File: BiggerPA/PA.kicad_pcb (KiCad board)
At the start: 2 copper layers, 100 x 100 mm, 105 parts, among them J1 Conn_Coaxial, J10 Conn_01x01, J2 Conn_01x02, J27 Conn_01x01, J28 Conn_01x01, J3 Conn_Coaxial, J4 Conn_01x02, J5 Conn_01x02, J6 Conn_01x01, J7 Conn_01x01, J8 Conn_01x01, J9 Conn_01x01, Q1 2N3906, Q10 IRF510N, Q11 IRF510N, Q12 IRF510N, Q13 IRF510N, Q14 IRF510N, Q15 IRF510N, Q18 TIP42, Q19 TIP42, Q2 IRF510N, Q20 TIP42, Q3 IRF510N, Q4 2N3906, Q5 TIP42, Q6 IRF510N, Q7 IRF510N, Q8 IRF510N, Q9 IRF510N, T1 Transformer_1P1Sdotted, T2 Transformer_1P1Sdotted, T3 Transformer_1P1Sdotted

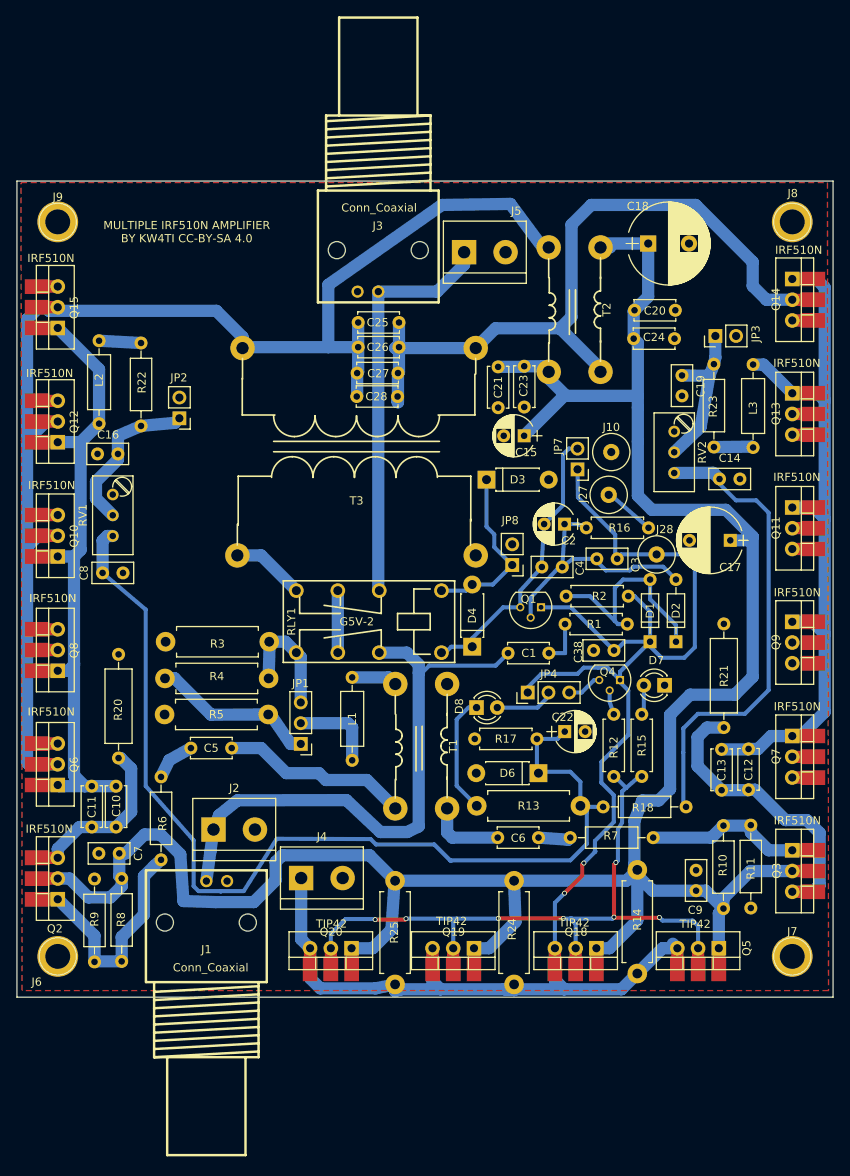
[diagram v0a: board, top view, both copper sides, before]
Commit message: Added series inductor to gates
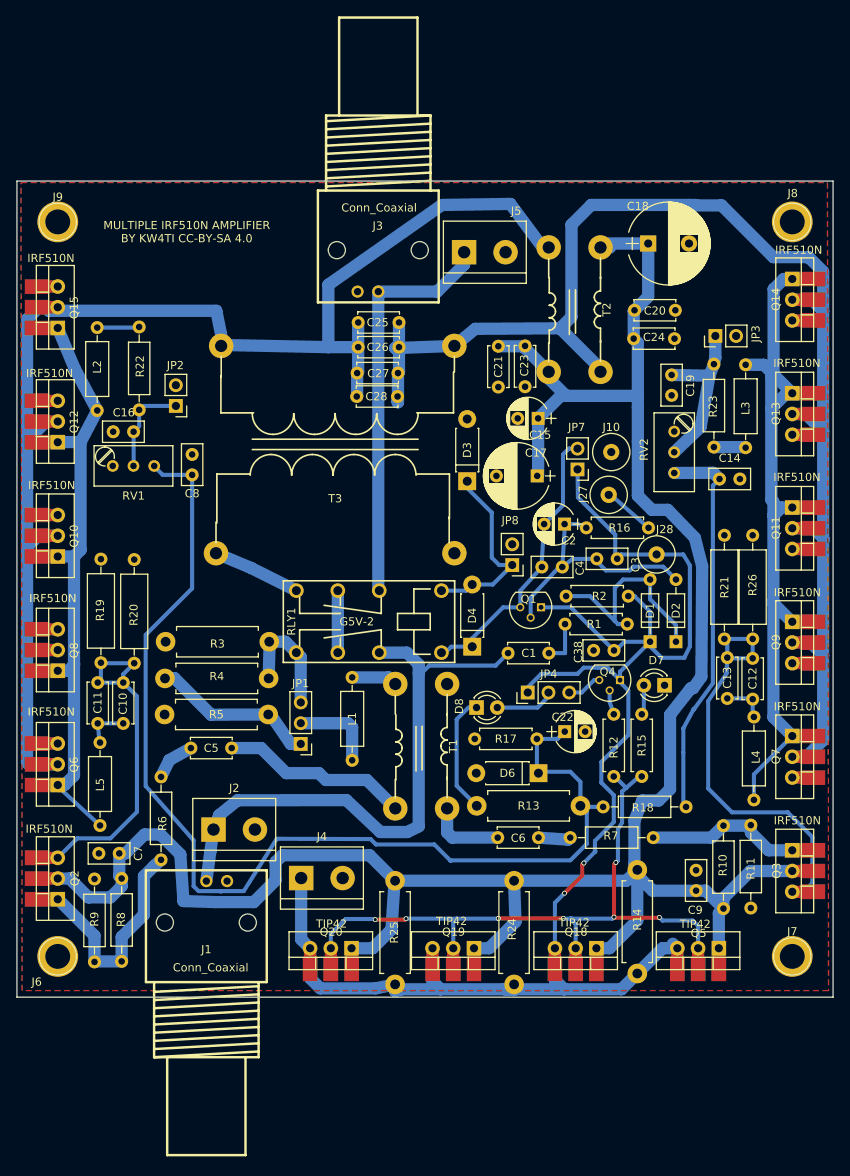
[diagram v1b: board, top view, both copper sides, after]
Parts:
- added L4: L, Inductors_THT:L_Axial_L6.6mm_D2.7mm_P10.16mm_Horizontal_Vishay_IM-2, F.Cu at (130.3, 105.7)
- added L5: L, Inductors_THT:L_Axial_L6.6mm_D2.7mm_P10.16mm_Horizontal_Vishay_IM-2, F.Cu at (50.2, 108.8)
- added R19: 51R, Resistors_THT:R_Axial_DIN0309_L9.0mm_D3.2mm_P12.70mm_Horizontal, F.Cu at (50.3, 99.0)
- added R26: 51R, Resistors_THT:R_Axial_DIN0309_L9.0mm_D3.2mm_P12.70mm_Horizontal, F.Cu at (130.1, 96.1)
- moved C17 24.9 mm to (103.7, 76.1)
- moved C8 16.3 mm to (61.5, 76.0), turned to 90 degrees
- moved R20 11.8 mm to (54.4, 99.1)
- moved R21 10.9 mm to (126.7, 96.1)
- moved C10 7.75 mm to (53.0, 106.5), turned to 90 degrees
- moved C11 7.73 mm to (49.9, 106.5), turned to 90 degrees
- moved C13 6.28 mm to (127.0, 103.4), turned to 90 degrees
- moved C12 6.12 mm to (130.1, 103.5), turned to 90 degrees
- moved RV1 3.51 mm to (51.7, 74.9), turned to 180 degrees
- moved C16 3.33 mm to (54.3, 70.7)
- moved C15 2.74 mm to (103.9, 69.1)
- moved T3 2.63 mm to (79.0, 72.9)
- moved C21 2.52 mm to (99.0, 60.2)
- moved C23 2.49 mm to (102.3, 60.2)
- moved D3 2.37 mm to (95.2, 76.8), turned to 90 degrees
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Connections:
- L2 pad 2: Net-(C10-Pad1) -> Net-(L2-Pad2)
- L3 pad 2: Net-(C12-Pad1) -> Net-(L3-Pad2)
- Q10 pad 1: Net-(C10-Pad1) -> Net-(L2-Pad2)
- Q11 pad 1: Net-(C12-Pad1) -> Net-(L3-Pad2)
- Q12 pad 1: Net-(C10-Pad1) -> Net-(L2-Pad2)
- Q13 pad 1: Net-(C12-Pad1) -> Net-(L3-Pad2)
- Q14 pad 1: Net-(C12-Pad1) -> Net-(L3-Pad2)
- Q15 pad 1: Net-(C10-Pad1) -> Net-(L2-Pad2)
- Q6 pad 1: Net-(C10-Pad1) -> Net-(L2-Pad2)
- Q7 pad 1: Net-(C12-Pad1) -> Net-(L3-Pad2)
- Q8 pad 1: Net-(C10-Pad1) -> Net-(L2-Pad2)
- Q9 pad 1: Net-(C12-Pad1) -> Net-(L3-Pad2)
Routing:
- net Net-(L3-Pad2): track 0.00 -> 97.9 mm
- net Net-(C12-Pad1): track 98.3 -> 5.40 mm
- net Net-(L2-Pad2): track 0.00 -> 86.7 mm
- net Net-(C25-Pad2): track 97.8 -> 182.1 mm
- net Net-(C10-Pad1): track 87.3 -> 5.51 mm
- net Net-(C10-Pad2): track 21.9 -> 43.9 mm
- net Net-(C12-Pad2): track 38.3 -> 54.5 mm
- net +5V: track 126.7 -> 138.3 mm
- net Net-(C14-Pad1): track 57.8 -> 48.4 mm
- net PASUPPLY: track 306.1 -> 296.8 mm
- net Net-(C16-Pad1): track 19.7 -> 11.9 mm
- net GND: track 22.9 -> 25.4 mm
- net AMPOUTPUT: track 9.02 -> 10.9 mm
- net Net-(D3-Pad1): track 21.7 -> 23.5 mm
- net Net-(C19-Pad1): track 19.2 -> 20.5 mm
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
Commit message: Added Filter
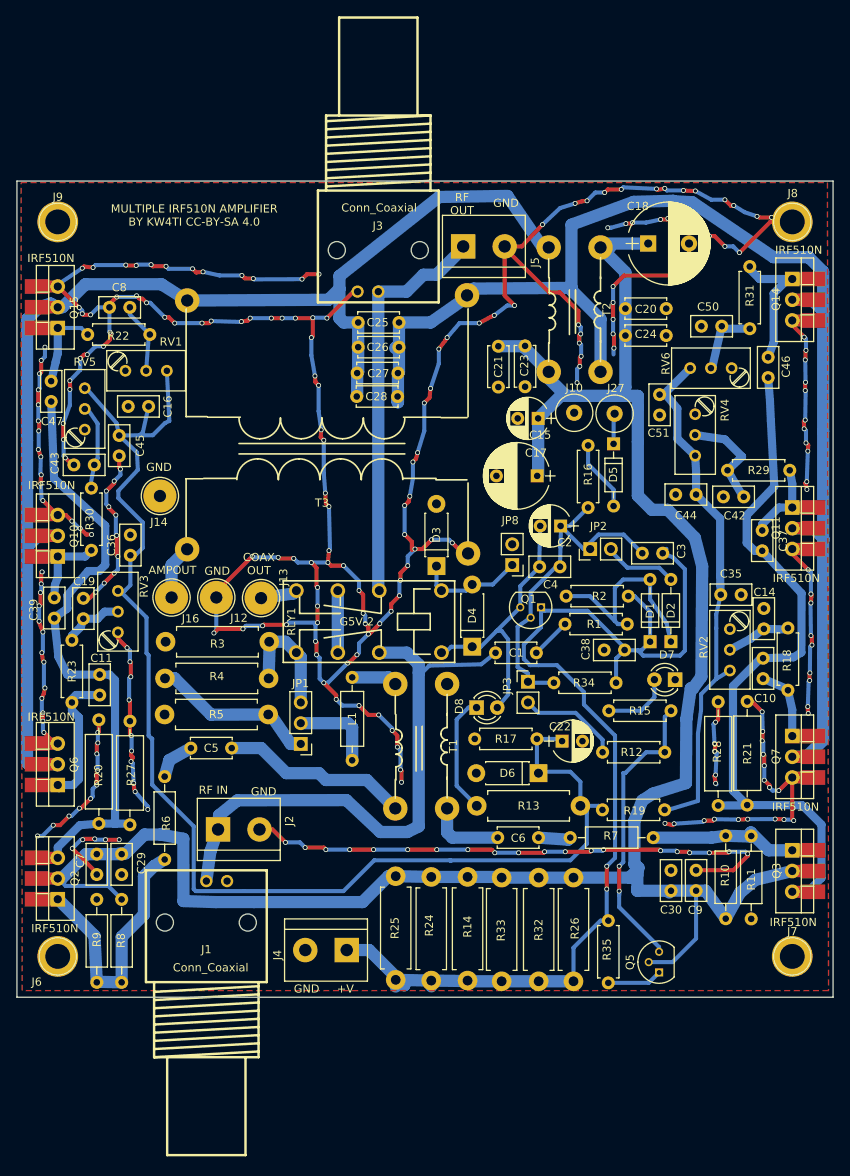
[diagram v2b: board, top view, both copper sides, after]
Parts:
- removed C12, C13: 100 nF, Capacitors_THT:C_Disc_D5.0mm_W2.5mm_P5.00mm
- removed J28: Conn_01x01, Connectors:1pin
- removed JP4: Jumper_NC_Dual, Pin_Headers:Pin_Header_Straight_1x03_Pitch2.54mm
- removed JP7: Jumper_NC_Small, Pin_Headers:Pin_Header_Straight_1x02_Pitch2.54mm
- removed L2, L3, L4, L5: L, Inductors_THT:L_Axial_L6.6mm_D2.7mm_P10.16mm_Horizontal_Vishay_IM-2
- removed Q12, Q13, Q8, Q9: IRF510N, PA:TO-220-3_Vertical_WithPads
- removed Q18, Q19, Q20: TIP42, PA:TO-220-3_Vertical_WithPads
- removed Q4: 2N3906, TO_SOT_Packages_THT:TO-92_Molded_Narrow
- added C29: 100 nF, Capacitors_THT:C_Disc_D5.0mm_W2.5mm_P2.50mm, F.Cu at (52.8, 125.0)
- added C30: 100 nF, Capacitors_THT:C_Disc_D5.0mm_W2.5mm_P2.50mm, F.Cu at (120.1, 124.5)
- added C35: 100 nF, Capacitors_THT:C_Disc_D5.0mm_W2.5mm_P2.50mm, F.Cu at (126.2, 90.7)
- added C36: 100 nF, Capacitors_THT:C_Disc_D5.0mm_W2.5mm_P2.50mm, F.Cu at (53.9, 85.9)
- added C37: 330 pF, Capacitors_THT:C_Disc_D5.0mm_W2.5mm_P2.50mm, F.Cu at (131.3, 82.8)
- added C39: 330 pF, Capacitors_THT:C_Disc_D5.0mm_W2.5mm_P2.50mm, F.Cu at (44.6, 91.1)
- added C42: 100 nF, Capacitors_THT:C_Disc_D5.0mm_W2.5mm_P2.50mm, F.Cu at (129.1, 78.7)
- added C43: 100 nF, Capacitors_THT:C_Disc_D5.0mm_W2.5mm_P2.50mm, F.Cu at (49.5, 74.8)
- added C44: 100 nF, Capacitors_THT:C_Disc_D5.0mm_W2.5mm_P2.50mm, F.Cu at (123.2, 78.4)
- added C45: 100 nF, Capacitors_THT:C_Disc_D5.0mm_W2.5mm_P2.50mm, F.Cu at (52.5, 71.2)
- added C46: 330 pF, Capacitors_THT:C_Disc_D5.0mm_W2.5mm_P2.50mm, F.Cu at (132.0, 61.6)
- added C47: 330 pF, Capacitors_THT:C_Disc_D5.0mm_W2.5mm_P2.50mm, F.Cu at (44.2, 64.5)
- added C50: 100 nF, Capacitors_THT:C_Disc_D5.0mm_W2.5mm_P2.50mm, F.Cu at (126.4, 57.8)
- added C51: 100 nF, Capacitors_THT:C_Disc_D5.0mm_W2.5mm_P2.50mm, F.Cu at (118.7, 66.2)
- added D5: 1N4148, Diodes_THT:D_DO-35_SOD27_P7.62mm_Horizontal, F.Cu at (113.1, 72.2)
- added J12: Conn_01x01, Connectors:1pin, F.Cu at (64.4, 91.0)
- added J13: Conn_01x01, Connectors:1pin, F.Cu at (69.9, 91.1)
- added J14: Conn_01x01, Connectors:1pin, F.Cu at (57.5, 78.6)
- added J16: Conn_01x01, Connectors:1pin, F.Cu at (58.9, 91.0)
- added R27: 51R, Resistors_THT:R_Axial_DIN0309_L9.0mm_D3.2mm_P12.70mm_Horizontal, F.Cu at (53.8, 118.9)
- added R28: 51R, Resistors_THT:R_Axial_DIN0309_L9.0mm_D3.2mm_P12.70mm_Horizontal, F.Cu at (125.9, 116.5)
- added R29: 10k, Resistors_THT:R_Axial_DIN0207_L6.3mm_D2.5mm_P7.62mm_Horizontal, F.Cu at (127.1, 75.4)
- added R30: 10k, Resistors_THT:R_Axial_DIN0207_L6.3mm_D2.5mm_P7.62mm_Horizontal, F.Cu at (49.1, 77.6)
- added R31: 10k, Resistors_THT:R_Axial_DIN0207_L6.3mm_D2.5mm_P7.62mm_Horizontal, F.Cu at (129.8, 58.1)
- added R32: 0R2, Resistors_THT:R_Axial_DIN0411_L9.9mm_D3.6mm_P12.70mm_Horizontal, F.Cu at (103.9, 125.3)
- added R33: 0R2, Resistors_THT:R_Axial_DIN0411_L9.9mm_D3.6mm_P12.70mm_Horizontal, F.Cu at (99.4, 125.3)
- added R34: 10k, Resistors_THT:R_Axial_DIN0207_L6.3mm_D2.5mm_P7.62mm_Horizontal, F.Cu at (113.4, 101.5)
- added R35: 470R, Resistors_THT:R_Axial_DIN0207_L6.3mm_D2.5mm_P7.62mm_Horizontal, F.Cu at (112.5, 130.6)
- added RV3: 10k, Potentiometers:Potentiometer_Trimmer_Bourns_3296W, F.Cu at (52.4, 95.3)
- added RV4: 10k, Potentiometers:Potentiometer_Trimmer_Bourns_3296W, F.Cu at (123.1, 68.6)
- added RV5: 10k, Potentiometers:Potentiometer_Trimmer_Bourns_3296W, F.Cu at (48.3, 70.5)
- added RV6: 10k, Potentiometers:Potentiometer_Trimmer_Bourns_3296W, F.Cu at (127.6, 62.9)
- C10, C11: value 100 nF -> 330 pF; footprint Capacitors_THT:C_Disc_D5.0mm_W2.5mm_P5.00mm -> Capacitors_THT:C_Disc_D5.0mm_W2.5mm_P2.50mm
- C15: value 1 uH -> 1 uF
- C17, C22: value 10 uH -> 10 uF
- C18: value 100 uH -> 100 uF
- C2: value 2.2 uH -> 2.2 uF
- Q5: value TIP42 -> 2N3906; footprint PA:TO-220-3_Vertical_WithPads -> TO_SOT_Packages_THT:TO-92_Molded_Narrow
- R12: value 10k -> 220R
- R13: value 2k4 -> 470R
- R18: value 0R -> 10k; footprint Resistors_THT:R_Axial_DIN0207_L6.3mm_D2.5mm_P10.16mm_Horizontal -> Resistors_THT:R_Axial_DIN0207_L6.3mm_D2.5mm_P7.62mm_Horizontal
- R19: value 51R -> 0R; footprint Resistors_THT:R_Axial_DIN0309_L9.0mm_D3.2mm_P12.70mm_Horizontal -> Resistors_THT:R_Axial_DIN0207_L6.3mm_D2.5mm_P7.62mm_Horizontal
- R22, R23: value 100R -> 10k; footprint Resistors_THT:R_Axial_DIN0207_L6.3mm_D2.5mm_P10.16mm_Horizontal -> Resistors_THT:R_Axial_DIN0207_L6.3mm_D2.5mm_P7.62mm_Horizontal
- R26: value 51R -> 0R2; footprint Resistors_THT:R_Axial_DIN0309_L9.0mm_D3.2mm_P12.70mm_Horizontal -> Resistors_THT:R_Axial_DIN0411_L9.9mm_D3.6mm_P12.70mm_Horizontal
- moved R23 82.1 mm to (46.7, 96.3), turned to 270 degrees
- moved C10 78.6 mm to (131.4, 101.0)
- moved C19 78.0 mm to (48.1, 93.6), turned to 90 degrees
- moved R19 71.4 mm to (119.4, 117.0), turned to 180 degrees
- moved JP2 53.7 mm to (110.2, 85.1), turned to 90 degrees
- moved JP3 48.2 mm to (102.6, 101.3), turned to 0 degrees
- moved R26 36.6 mm to (108.2, 125.3), turned to 270 degrees
- moved R18 25.2 mm to (134.5, 94.8), turned to 270 degrees
- moved RV2 25.1 mm to (127.4, 94.9)
- moved C8 21.9 mm to (53.8, 55.5), turned to 180 degrees
- moved R14 20.8 mm to (95.2, 125.3)
- moved R21 20.5 mm to (129.5, 116.5)
- moved R20 20.1 mm to (50.0, 118.7)
- moved C14 19.2 mm to (131.5, 94.9), turned to 90 degrees
- moved R16 12.5 mm to (110.0, 72.4), turned to 270 degrees
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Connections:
- C11 pad 1: Net-(C10-Pad1) -> Net-(C11-Pad1)
- C11 pad 2: Net-(C10-Pad2) -> Net-(C11-Pad2)
- C16 pad 1: Net-(C16-Pad1) -> +5V
- C3 pad 1: +28V -> +12V
- C38 pad 1: +28V -> +12V
- C8 pad 1: +5V -> Net-(C8-Pad1)
- D1 pad 1: +28V -> +12V
- D2 pad 2: Net-(C2-Pad1) -> Net-(D2-Pad2)
- D8 pad 2: Net-(D8-Pad2) -> Net-(C2-Pad2)
- J27 pad 1: Net-(J27-Pad1) -> Net-(D5-Pad1)
- J4 pad 1: +28V -> +12V
- JP2 pad 1: Net-(C16-Pad1) -> Net-(C2-Pad1)
- JP2 pad 2: GND -> Net-(D2-Pad2)
- JP3 pad 1: Net-(C19-Pad1) -> Net-(C2-Pad1)
- JP3 pad 2: GND -> Net-(JP3-Pad2)
- Q1 pad 1: +28V -> +12V
- Q10 pad 1: Net-(L2-Pad2) -> Net-(C39-Pad1)
- Q11 pad 1: Net-(L3-Pad2) -> Net-(C37-Pad1)
- Q14 pad 1: Net-(L3-Pad2) -> Net-(C46-Pad1)
- Q15 pad 1: Net-(L2-Pad2) -> Net-(C47-Pad1)
- Q2 pad 3: Net-(C10-Pad2) -> Net-(C11-Pad2)
- Q3 pad 3: Net-(C12-Pad2) -> Net-(C10-Pad2)
- Q5 pad 1: PASUPPLY -> Net-(Q5-Pad1)
- Q5 pad 2: Net-(Q18-Pad2) -> PASUPPLY
- Q5 pad 3: +28V -> Net-(Q5-Pad3)
- Q6 pad 1: Net-(L2-Pad2) -> Net-(C11-Pad1)
- Q7 pad 1: Net-(L3-Pad2) -> Net-(C10-Pad1)
- R12 pad 1: Net-(Q18-Pad2) -> Net-(JP3-Pad2)
- R12 pad 2: Net-(Q4-Pad2) -> Net-(Q5-Pad3)
- R14 pad 2: +28V -> +12V
- R15 pad 1: Net-(Q18-Pad2) -> Net-(Q5-Pad3)
- R16 pad 1: Net-(J27-Pad1) -> Net-(D5-Pad2)
- R18 pad 2: +5V -> Net-(C10-Pad1)
- R19 pad 1: Net-(C10-Pad2) -> Net-(C35-Pad1)
- R19 pad 2: GND -> +5V
- R2 pad 1: +28V -> +12V
- R20 pad 1: Net-(C10-Pad2) -> Net-(C11-Pad2)
- R21 pad 1: Net-(C12-Pad2) -> Net-(C10-Pad2)
- R22 pad 1: Net-(L2-Pad1) -> Net-(C8-Pad1)
- R22 pad 2: Net-(C16-Pad1) -> Net-(C47-Pad1)
- R23 pad 1: Net-(L3-Pad1) -> Net-(C19-Pad1)
- R23 pad 2: Net-(C19-Pad1) -> Net-(C11-Pad1)
- R24 pad 2: +28V -> +12V
- R25 pad 2: +28V -> +12V
- R26 pad 1: Net-(C12-Pad2) -> PASUPPLY
- R26 pad 2: GND -> +12V
- RLY1 pad 8: AMPOUTPUT -> COAXOUT
- RV1 pad 2: Net-(C16-Pad1) -> Net-(C8-Pad1)
- RV2 pad 2: Net-(C19-Pad1) -> Net-(C14-Pad1)
- RV2 pad 3: Net-(C14-Pad1) -> Net-(C35-Pad1)
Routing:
- net GND: track 25.4 -> 690.5 mm, vias 0 -> 255
- net +28V: track 206.0 -> 0.00 mm, vias 2 -> 0
- net +12V: track 0.00 -> 139.0 mm, vias 0 -> 2
- net Net-(L3-Pad2): track 97.9 -> 0.00 mm
- net Net-(Q18-Pad2): track 90.5 -> 0.00 mm, vias 7 -> 0
- net Net-(L2-Pad2): track 86.7 -> 0.00 mm
- net Net-(C11-Pad2): track 0.00 -> 77.6 mm
- net Net-(C35-Pad1): track 0.00 -> 65.4 mm
- net Net-(C12-Pad2): track 54.5 -> 0.00 mm
- net Net-(C10-Pad2): track 43.9 -> 90.7 mm
- net Net-(C14-Pad1): track 48.4 -> 7.90 mm
- net Net-(Q5-Pad3): track 0.00 -> 36.2 mm, vias 0 -> 2
- net PASUPPLY: track 296.8 -> 267.8 mm
- net +5V: track 138.3 -> 163.7 mm
- net Net-(C11-Pad1): track 0.00 -> 19.6 mm
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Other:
- board text added: "+V"
- board text added: "AMPOUT"
- board text added: "COAX OUT"
- board text added: "GND"
- board text added: "RF IN"
- board text added: "RF OUT"
- board text removed: "TIP42"

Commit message: Changed to 7805 regulator
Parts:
- removed D6: 1N4744A, Diodes_THT:D_DO-41_SOD81_P7.62mm_Horizontal
- removed R13: 470R, Resistors_THT:R_Axial_DIN0411_L9.9mm_D3.6mm_P12.70mm_Horizontal
- added U1: LM7805_TO220, TO_SOT_Packages_THT:TO-220-3_Vertical, F.Cu at (100.2, 116.9)
- moved R12 1.48 mm to (112.2, 108.6)
- moved C22 0.22 mm to (106.9, 108.5)
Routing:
- net +5V: track 163.7 -> 158.9 mm
- net Net-(D8-Pad1): track 14.7 -> 16.8 mm
- net +12V: track 139.0 -> 140.8 mm
- net Net-(JP3-Pad2): track 12.6 -> 11.5 mm
- net Net-(Q5-Pad3): track 36.2 -> 35.1 mm
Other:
- board text added: "LM7805"

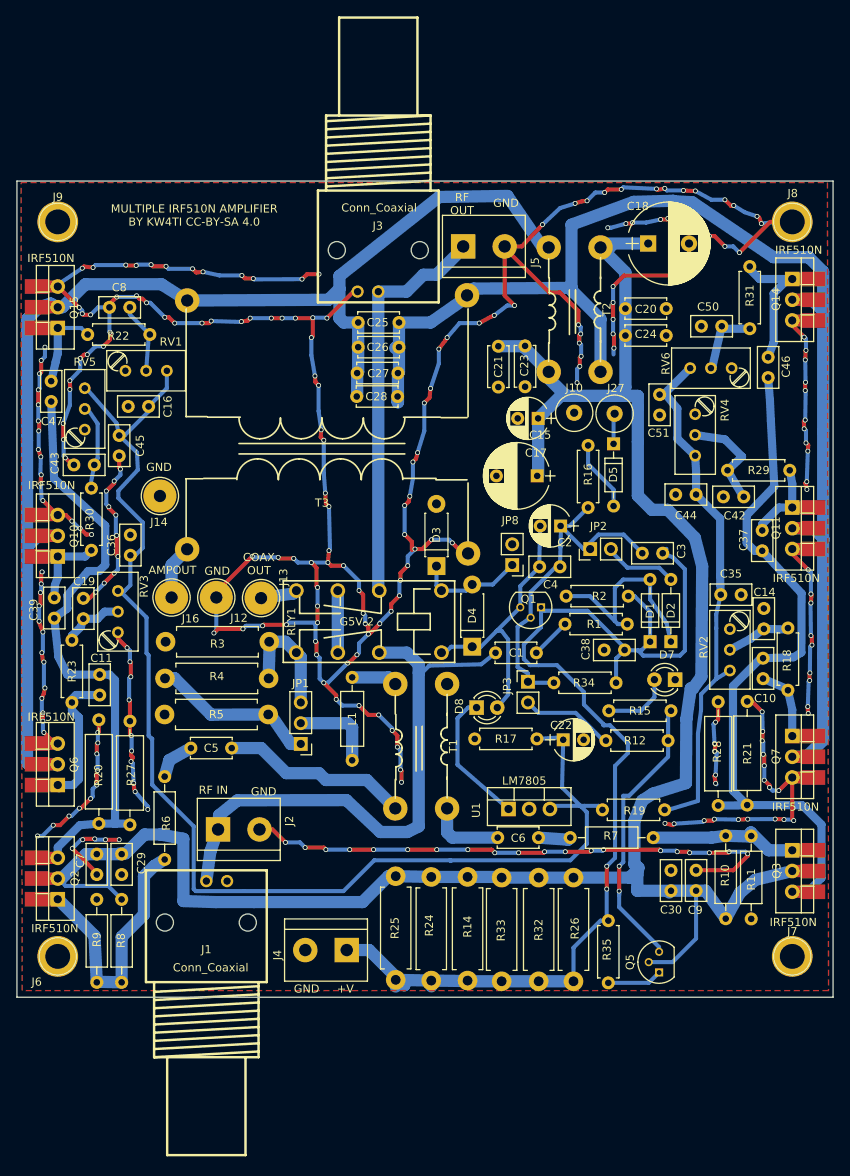
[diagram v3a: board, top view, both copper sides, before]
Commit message: Added gate resistors to BiggerPA
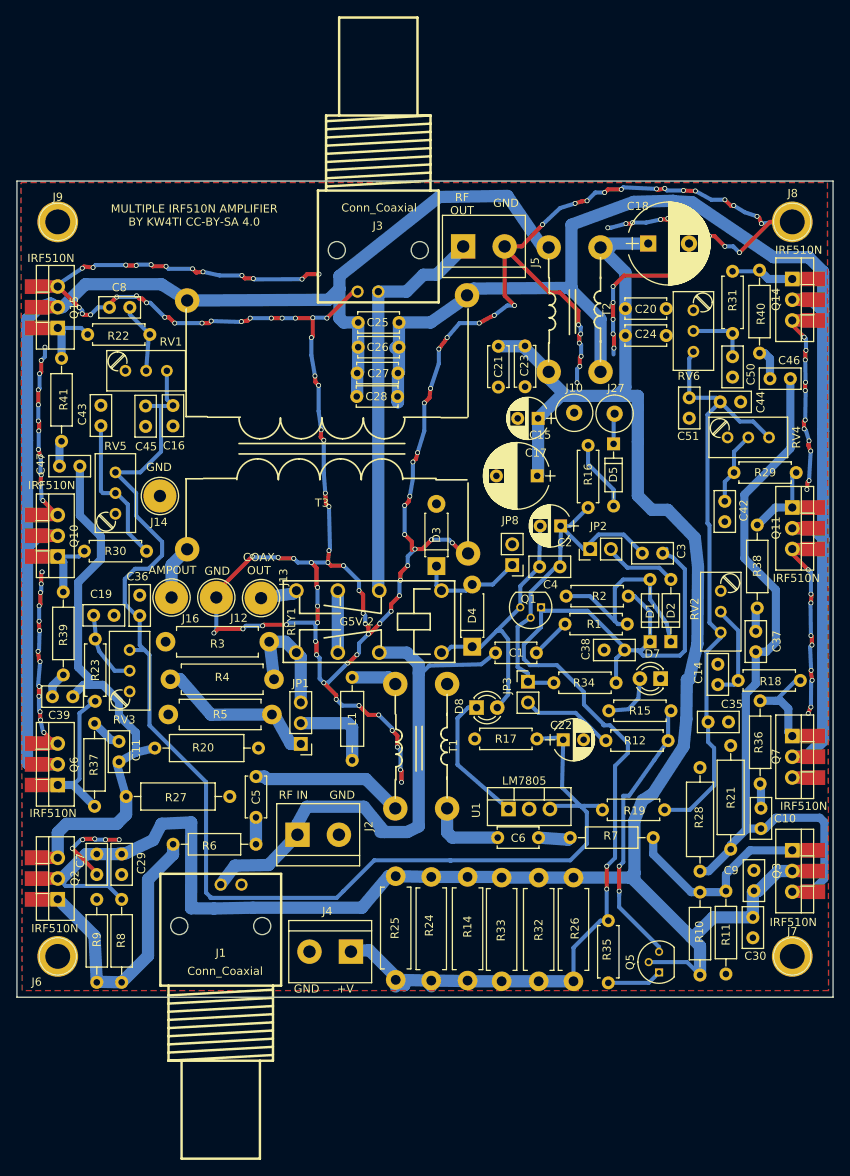
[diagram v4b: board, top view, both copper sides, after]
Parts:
- added R36: 4R7, Resistors_THT:R_Axial_DIN0207_L6.3mm_D2.5mm_P10.16mm_Horizontal, F.Cu at (131.1, 113.8)
- added R37: 4R7, Resistors_THT:R_Axial_DIN0207_L6.3mm_D2.5mm_P10.16mm_Horizontal, F.Cu at (49.5, 106.5)
- added R38: 4R7, Resistors_THT:R_Axial_DIN0207_L6.3mm_D2.5mm_P10.16mm_Horizontal, F.Cu at (130.7, 92.3)
- added R39: 4R7, Resistors_THT:R_Axial_DIN0207_L6.3mm_D2.5mm_P10.16mm_Horizontal, F.Cu at (45.7, 100.5)
- added R40: 4R7, Resistors_THT:R_Axial_DIN0207_L6.3mm_D2.5mm_P10.16mm_Horizontal, F.Cu at (131.0, 61.1)
- added R41: 4R7, Resistors_THT:R_Axial_DIN0207_L6.3mm_D2.5mm_P10.16mm_Horizontal, F.Cu at (45.5, 71.9)
- moved C10 15.9 mm to (131.2, 116.8), turned to 270 degrees
- moved C35 15.7 mm to (124.7, 106.3)
- moved R6 13.9 mm to (69.3, 121.3), turned to 180 degrees
- moved C37 12.4 mm to (130.5, 95.2)
- moved C39 12.1 mm to (44.3, 103.2), turned to 0 degrees
- moved C44 11.7 mm to (126.2, 67.1), turned to 0 degrees
- moved C5 11.6 mm to (69.3, 118.0), turned to 90 degrees
- moved R20 11.5 mm to (56.9, 109.5), turned to 0 degrees
- moved RV5 11.0 mm to (52.1, 80.8)
- moved C9 10.8 mm to (130.2, 132.7), turned to 90 degrees
- moved C47 10.5 mm to (45.2, 74.9), turned to 0 degrees
- moved R30 10.3 mm to (55.9, 85.3), turned to 180 degrees
- moved C30 10.2 mm to (130.3, 124.5)
- moved J2 9.75 mm to (74.4, 120.1)
- moved C14 8.86 mm to (125.9, 101.7)
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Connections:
- Q10 pad 1: Net-(C39-Pad1) -> Net-(Q10-Pad1)
- Q11 pad 1: Net-(C37-Pad1) -> Net-(Q11-Pad1)
- Q14 pad 1: Net-(C46-Pad1) -> Net-(Q14-Pad1)
- Q15 pad 1: Net-(C47-Pad1) -> Net-(Q15-Pad1)
- Q6 pad 1: Net-(C11-Pad1) -> Net-(Q6-Pad1)
- Q7 pad 1: Net-(C10-Pad1) -> Net-(Q7-Pad1)
- R18 pad 2: Net-(C10-Pad1) -> Net-(Q7-Pad1)
- R22 pad 2: Net-(C47-Pad1) -> Net-(Q15-Pad1)
- R23 pad 2: Net-(C11-Pad1) -> Net-(Q6-Pad1)
- R29 pad 2: Net-(C37-Pad1) -> Net-(Q11-Pad1)
- R30 pad 2: Net-(C39-Pad1) -> Net-(Q10-Pad1)
- R31 pad 2: Net-(C46-Pad1) -> Net-(Q14-Pad1)
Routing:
- net GND: track 690.8 -> 483.2 mm, vias 255 -> 170
- net Net-(Q6-Pad1): track 0.00 -> 21.3 mm
- net Net-(C11-Pad1): track 19.6 -> 3.85 mm
- net Net-(C46-Pad1): track 19.5 -> 4.03 mm
- net Net-(Q7-Pad1): track 0.00 -> 14.5 mm
- net Net-(Q11-Pad1): track 0.00 -> 12.2 mm
- net Net-(Q14-Pad1): track 0.00 -> 10.9 mm
- net Net-(Q10-Pad1): track 0.00 -> 10.7 mm
- net Net-(Q15-Pad1): track 0.00 -> 10.5 mm
- net Net-(C47-Pad1): track 13.1 -> 3.15 mm
- net Net-(C35-Pad1): track 65.4 -> 75.3 mm
- net Net-(C37-Pad1): track 12.4 -> 2.94 mm
- net Net-(C10-Pad1): track 12.1 -> 3.04 mm
- net Net-(C39-Pad1): track 12.1 -> 3.22 mm
- net Net-(C43-Pad1): track 10.6 -> 18.6 mm
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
